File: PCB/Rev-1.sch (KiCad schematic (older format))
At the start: 136 parts, among them SW1 SW_Push, U1 ATmega32U4-AU, Y1 16MHz

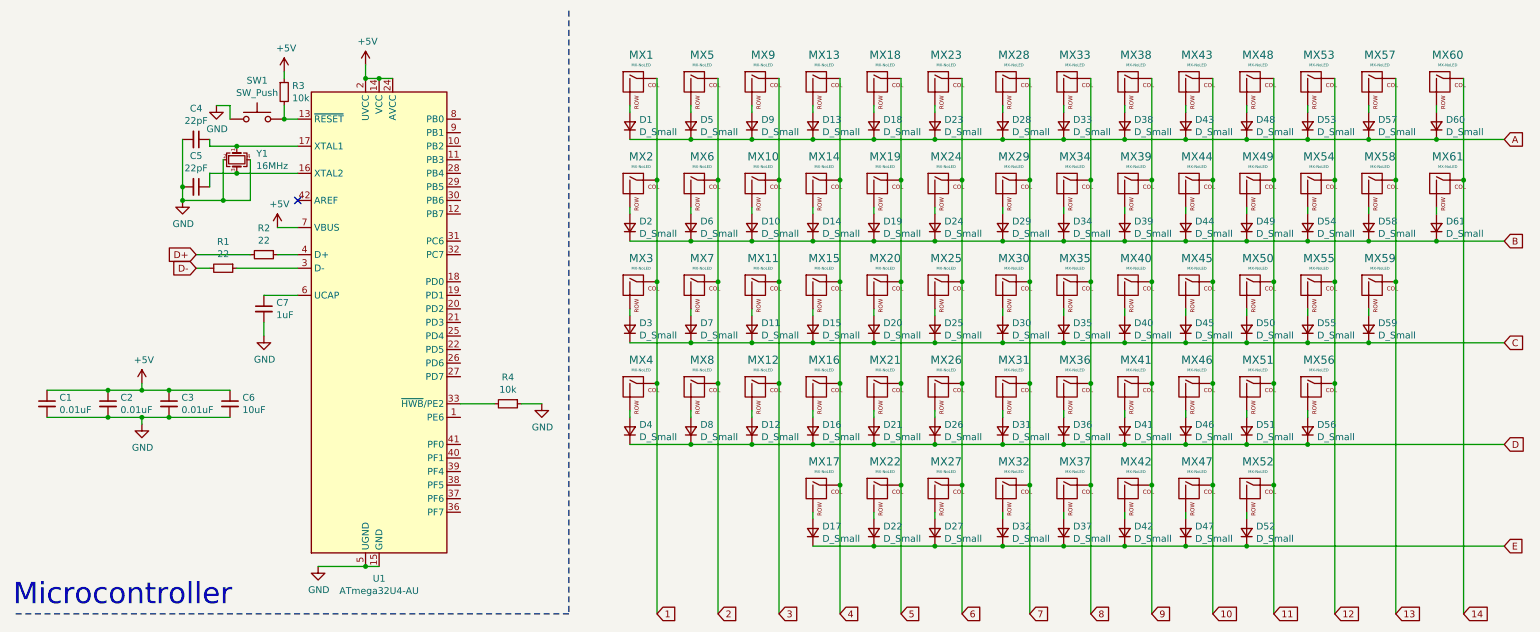
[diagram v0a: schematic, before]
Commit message: Started work on pcb layout, currently adding in proper key sizes.
Signed-off-by: Oscar <oscarwebb08@gmail.com>
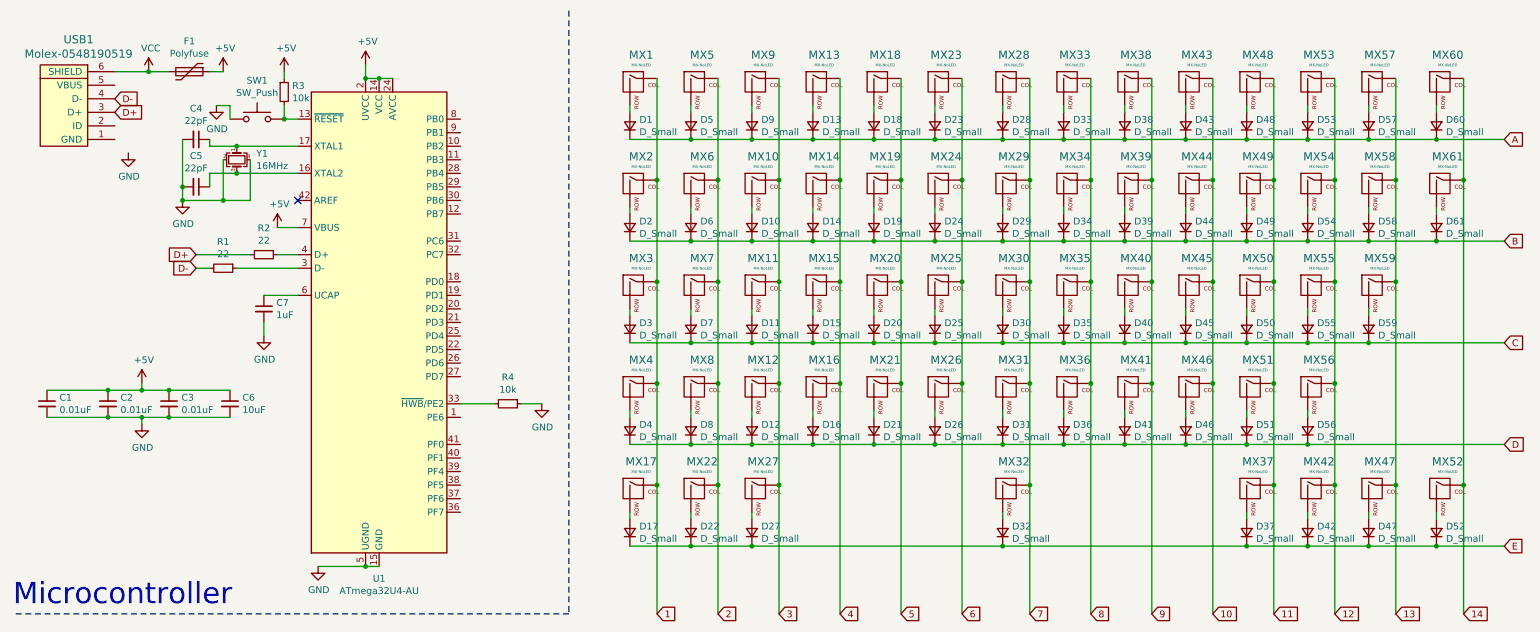
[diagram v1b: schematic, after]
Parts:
- added F1: Polyfuse, Fuse:Fuse_1206_3216Metric, symbol Device:Polyfuse
- added USB1: Molex-0548190519, random-keyboard-parts:Molex-0548190589, symbol random-keyboard-parts:Molex-0548190519
- MX17, MX22, MX27, MX37, MX42, MX47, MX52: footprint Kailh_Choc:KailhChoc-1U -> Kailh_Choc:KailhChoc-1.25U
- MX32: footprint Kailh_Choc:KailhChoc-1U -> Kailh_Choc:KailhChoc-1.75U
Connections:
- net +5V: now also F1.1
- net 1: now also MX17.1 (COL)
- net 10: no longer MX47.1 (COL)
- net 11: now also MX37.1 (COL); no longer MX52.1 (COL)
- net 12: now also MX42.1 (COL)
- net 13: now also MX47.1 (COL)
- net 14: now also MX52.1 (COL)
- net 2: now also MX22.1 (COL)
- net 3: now also MX27.1 (COL)
- net 4: no longer MX17.1 (COL)
- net 5: no longer MX22.1 (COL)
- net 6: no longer MX27.1 (COL)
- net 8: no longer MX37.1 (COL)
- net 9: no longer MX42.1 (COL)
- net D+: now also USB1.3 (D+)
- net D-: now also USB1.4 (D-)
- new net VCC: F1.2, USB1.6 (SHIELD)
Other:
- moved on the sheet: D17, D22, D27, D37, D42, D47, D52, MX17, MX22, MX27, MX37, MX42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
